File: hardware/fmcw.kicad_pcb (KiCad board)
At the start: 4 copper layers, 123.2 x 49.5 mm, 450 parts, among them CON2 BARREL_JACK, J1 SD_Card, J2 USB_B_Micro, P1 SMA, P10 CONN_01X01, P11 CONN_01X01, P12 CONN_01X01, P13 CONN_01X01, P14 CONN_01X01, P15 CONN_01X01, P16 CONN_01X01, P2 SMA, P3 CONN_02X04, P4 CONN_02X04, P5 CONN_01X01, P6 CONN_01X01, P7 CONN_01X01, P8 CONN_01X01, P9 CONN_01X01, Q1 RE1C002UN, Q2 DNP(RE1C002UN), SW2 SW_PUSH, U1 ADF4158, U10 HMC431LP4, U11 SKY65404, U12 PAT1220-6dB, U13 TRF37A73, U14 FT2232H, U15 SMA, U16 SKY65404, U17 SE5004L, U18 TPS5420D, U19 TPS5420D, U2 LP5907-1.8, U20 LP5907-3.0, U21 LP2985A-10DBVR, U22 TPS7A91, U23 TPS7A91, U24 TPS7A91, U25 MIC5301-3.3, U26 5400BL15B050E, U27 5400BL15B050E, U28 5400BL15B050E, U29 ADL5802, U3 PAT1220-6dB, U31 93LCxxB, U32 TPS7A7200RGW, U34 ADA4940-2, U35 ADA4940-2, U37 SE2567L, U38 TPS7A91, U39 LP5907-3.0, U4 KT2520K, U40 W25Q32JV, U5 NC7S04P5X, U6 NB3N551, U7 TLV172DCK, U8 LTC2292, U9 TRF37A73, Y1 ABM10-167-12.000MHZ-T3

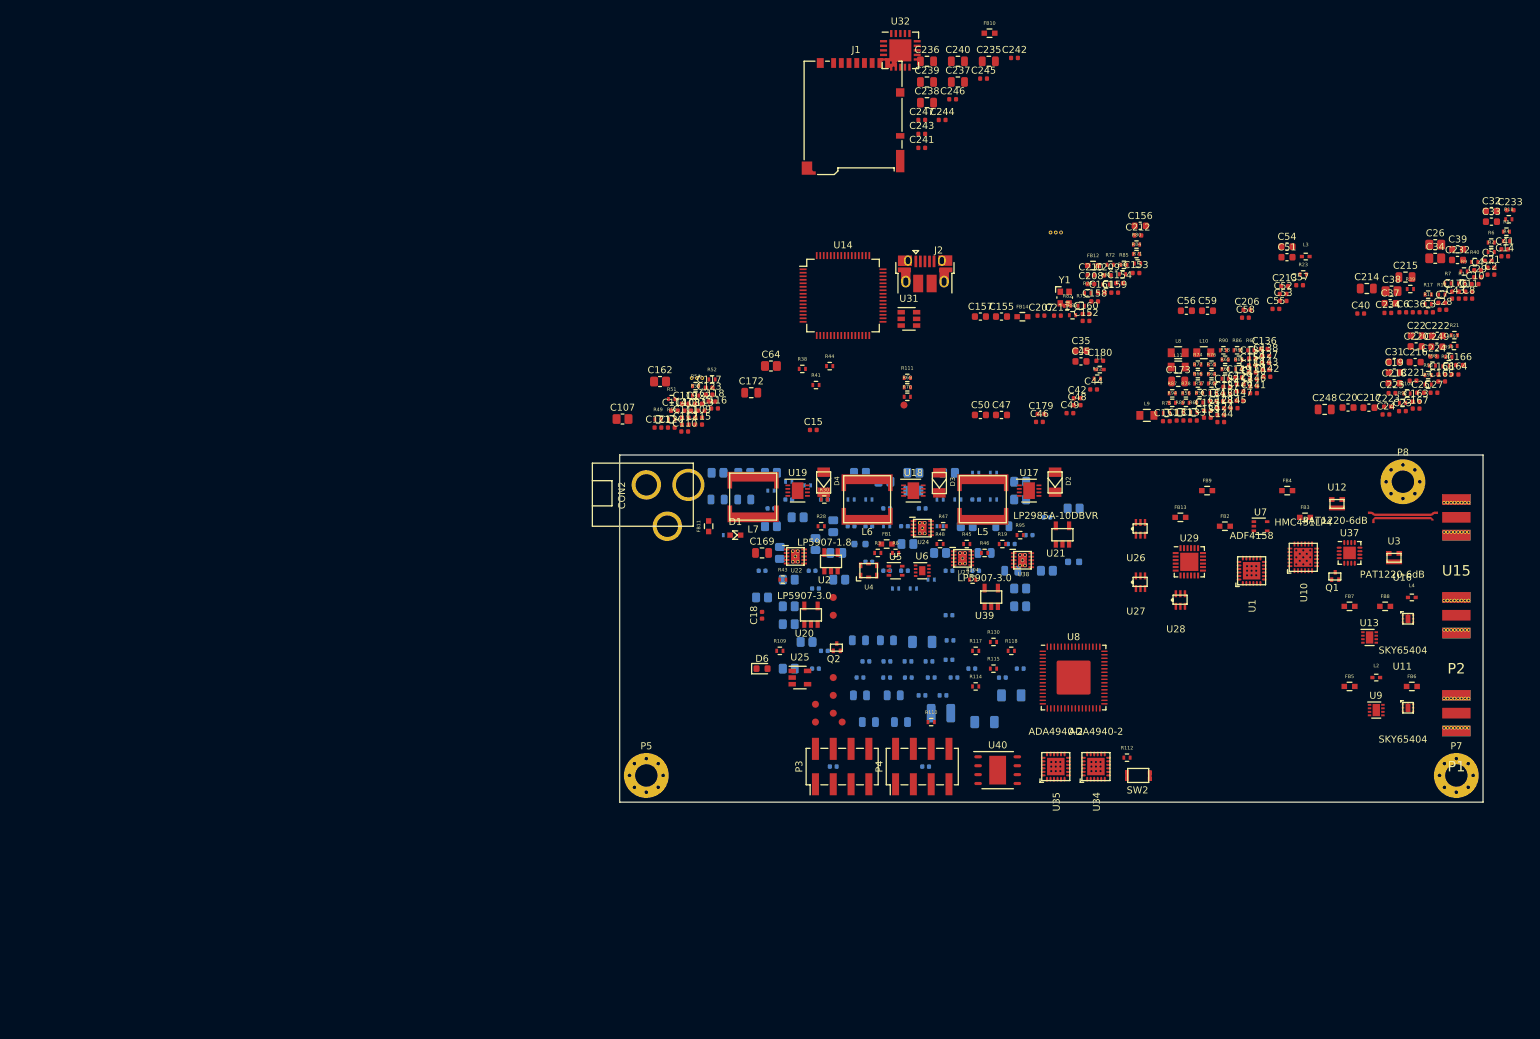
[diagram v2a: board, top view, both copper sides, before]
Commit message: Added MFNs to components.
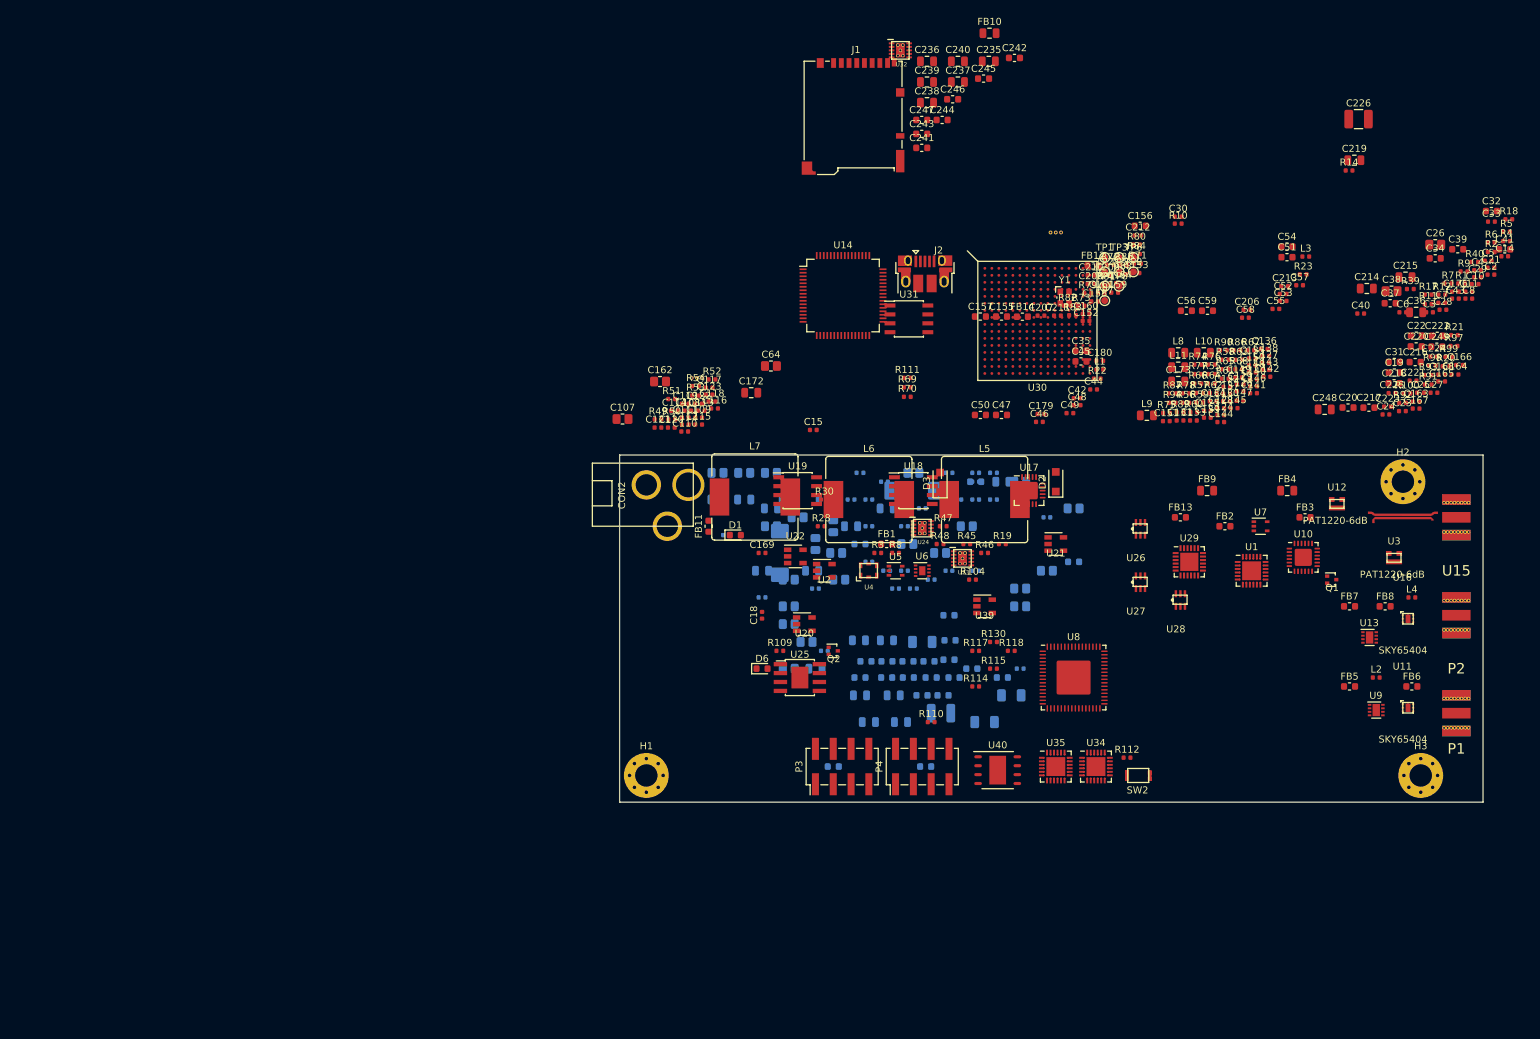
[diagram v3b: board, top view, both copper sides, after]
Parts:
- removed C227, C230: 10u, Capacitor_SMD:C_0805_2012Metric
- removed C228: 100n, Capacitor_SMD:C_0402_1005Metric
- removed C229: 10n, Capacitor_SMD:C_0402_1005Metric
- removed C231: DNP, Capacitor_SMD:C_0805_2012Metric
- removed C232: 2.2u, Capacitor_SMD:C_0603_1608Metric
- removed C233, C234: 100p, Capacitor_SMD:C_0402_1005Metric
- removed D4: SS13FL, fmcw:SOD-123F
- removed P10, P11, P12, P13, P14, P15, P16, P6, P9: CONN_01X01, fmcw:TP_1.00
- removed P5, P7, P8: CONN_01X01, fmcw:MountingHole_3.2mm_M3_Pad_Via_mod
- removed R101: DNP, fmcw:R_0402b
- removed R103: 0, fmcw:R_0402b
- removed R34, R36: 4.99k, fmcw:R_0402b
- removed R35: 1k, fmcw:R_0402b
- removed R37: 590, fmcw:R_0402b
- removed R38: 33, fmcw:R_0402b
- removed R41: 56, fmcw:R_0402b
- removed R42: 100, fmcw:R_0402b
- removed R43: 10.5k, fmcw:R_0402b
- removed R44: 2k, fmcw:R_0402b
- removed R95: 1.47k, fmcw:R_0402b
- removed U37: SE2567L, Package_DFN_QFN:QFN-16-1EP_3x3mm_P0.5mm_EP1.8x1.8mm
- removed U38: TPS7A91, fmcw:SON-10_2.5x2.5mm
- added C219: DNP, Capacitor_SMD:C_0805_2012Metric, F.Cu at (215.3, 32.9)
- added C226: 47u, Capacitor_SMD:C_1210_3225Metric, F.Cu at (215.9, 27.0)
- added C30: 10p, Capacitor_SMD:C_0402_1005Metric, F.Cu at (190.2, 40.9)
- added H1: MountingHole_Pad, MountingHole:MountingHole_3.2mm_M3_Pad_Via, F.Cu at (114.3, 120.7)
- added H2: MountingHole_Pad, MountingHole:MountingHole_3.2mm_M3_Pad_Via, F.Cu at (222.2, 78.7)
- added H3: MountingHole_Pad, MountingHole:MountingHole_3.2mm_M3_Pad_Via, F.Cu at (224.8, 120.7)
- added R10: 10k, Resistor_SMD:R_0402_1005Metric, F.Cu at (190.2, 41.9)
- added R14: 10k, Resistor_SMD:R_0402_1005Metric, F.Cu at (214.6, 34.3)
- added TP1: TestPoint, TestPoint:TestPoint_Pad_D1.0mm, F.Cu at (179.7, 46.7)
- added TP2: TestPoint, TestPoint:TestPoint_Pad_D1.0mm, F.Cu at (179.7, 48.8)
- added TP3: TestPoint, TestPoint:TestPoint_Pad_D1.0mm, F.Cu at (181.7, 46.7)
- added TP4: TestPoint, TestPoint:TestPoint_Pad_D1.0mm, F.Cu at (179.7, 50.8)
- added TP5: TestPoint, TestPoint:TestPoint_Pad_D1.0mm, F.Cu at (181.7, 48.8)
- added TP6: TestPoint, TestPoint:TestPoint_Pad_D1.0mm, F.Cu at (183.8, 46.7)
- added TP7: TestPoint, TestPoint:TestPoint_Pad_D1.0mm, F.Cu at (179.7, 52.9)
- added TP8: TestPoint, TestPoint:TestPoint_Pad_D1.0mm, F.Cu at (181.7, 50.8)
- added TP9: TestPoint, TestPoint:TestPoint_Pad_D1.0mm, F.Cu at (183.8, 48.8)
- added U30: XC7A15T-FTG256, fmcw:FTG256, F.Cu at (170.1, 55.8)
- C100: value 10u -> 100n; footprint Capacitor_SMD:C_0805_2012Metric -> Capacitor_SMD:C_0402_1005Metric
- C103, C86: value DNP -> 10u
- C106: value 10u -> DNP
- C169: value DNP -> 10n; footprint Capacitor_SMD:C_0805_2012Metric -> Capacitor_SMD:C_0402_1005Metric
- C170, C171, C187, C189, C190, C191, C192, C193, C197, C198, C199, C200, C201, C202, C203, C204, C205, C241, C242, C243, C244, C245, C246, C247, C251, C41, C63, C66: footprint Capacitor_SMD:C_0402_1005Metric -> Capacitor_SMD:C_0603_1608Metric
- C175, C96: value DNP -> 10u; footprint Capacitor_SMD:C_0402_1005Metric -> Capacitor_SMD:C_0805_2012Metric
- C33: footprint Capacitor_SMD:C_0603_1608Metric -> Capacitor_SMD:C_0402_1005Metric
- C34: footprint Capacitor_SMD:C_0805_2012Metric -> Capacitor_SMD:C_0603_1608Metric
- C36, C65, C69, C73, C74, C75, C90: footprint Capacitor_SMD:C_0402_1005Metric -> Capacitor_SMD:C_0805_2012Metric
- C60, C61, C77, C78: footprint Capacitor_SMD:C_0805_2012Metric -> Capacitor_SMD:C_0402_1005Metric
- C79, C80: value 6TPH100MAEA -> 100u; footprint Capacitor_SMD:C_0805_2012Metric -> Capacitor_Tantalum_SMD:CP_EIA-7343-31_Kemet-D
- C82: value 10n -> 100n
- C83: value 100n -> 10u
- C84: value 10n -> 10u
- D1: value LED -> Red; footprint fmcw:LED_0603 -> LED_SMD:LED_0603_1608Metric
- D2, D3: footprint fmcw:SOD-123F -> Diode_SMD:D_SOD-123F
- D6: value LED -> Red
- FB1, FB12, FB13, FB14, FB2, FB3, FB5, FB6, FB7, FB8: value BLM18PG181SN1D -> BLM18PG181SH1D; footprint fmcw:C_0603b -> Inductor_SMD:L_0603_1608Metric
- FB10, FB4, FB9: footprint fmcw:C_0603b -> Inductor_SMD:L_0805_2012Metric
- FB11: value CIC21P101NE -> 74279228600; footprint fmcw:C_0603b -> Inductor_SMD:L_0603_1608Metric
- L1, L2, L3, L4: footprint fmcw:C_0402b -> Inductor_SMD:L_0402_1005Metric
- L10, L11, L8, L9: footprint fmcw:C_0805b -> Inductor_SMD:L_0805_2012Metric
- L5, L7: value SRR1210A-330M -> 33u; footprint fmcw:SRR6040A -> Inductor_SMD:L_Bourns_SRR1210A
- L6: value 33u (SRR6040A-330M) -> 33u; footprint fmcw:SRR6040A -> Inductor_SMD:L_Bourns_SRR1210A
- Q1, Q2: footprint fmcw:SOT-416 -> Package_TO_SOT_SMD:SOT-416
- R1, R100, R104, R109, R11, R110, R111, R112, R114, R115, R117, R118, R12, R13, R130, R15, R16, R17, R18, R19, R2, R20, R21, R22, R23, R24, R25, R26, R3, R39, R40, R45, R46, R47, R48, R49, R5, R50, R51, R52, R53, R54, R59, R6, R60, R61, R62, R63, R64, R65, R66, R67, R68, R69, R7, R70, R71, R72, R73, R74, R75, R76, R77, R78, R79, R8, R80, R81, R82, R83, R84, R85, R86, R87, R88, R89, R9, R90, R91, R92, R93, R94, R97, R98, R99: footprint fmcw:R_0402b -> Resistor_SMD:R_0402_1005Metric
- R27: value 100k -> 33; footprint fmcw:R_0402b -> Resistor_SMD:R_0402_1005Metric
- R28: value 2.55k -> 4.99k; footprint fmcw:R_0402b -> Resistor_SMD:R_0402_1005Metric
- R29: value 10.2k -> 20k; footprint fmcw:R_0402b -> Resistor_SMD:R_0402_1005Metric
- R30: value 280k -> 274k; footprint fmcw:R_0402b -> Resistor_SMD:R_0402_1005Metric
- R31: value 30.9k -> 30.1k; footprint fmcw:R_0402b -> Resistor_SMD:R_0402_1005Metric
- R32: value 4.99k -> 3.57k; footprint fmcw:R_0402b -> Resistor_SMD:R_0402_1005Metric
- R33: value 7.5k -> 1.15k; footprint fmcw:R_0402b -> Resistor_SMD:R_0402_1005Metric
- R4: value 3.1k -> 3.09k; footprint fmcw:R_0402b -> Resistor_SMD:R_0402_1005Metric
- R55, R56, R57, R58: value 550 -> 549; footprint fmcw:R_0402b -> Resistor_SMD:R_0402_1005Metric
- U1, U34, U35: footprint fmcw:VFQFN-24 -> Package_DFN_QFN:WQFN-24-1EP_4x4mm_P0.5mm_EP2.7x2.7mm
- U10: footprint fmcw:VQFN-24 -> Package_DFN_QFN:VQFN-24-1EP_4x4mm_P0.5mm_EP2.45x2.45mm
- U17: footprint Package_DFN_QFN:DFN-8-1EP_3x3mm_P0.5mm_EP1.66x2.38mm -> Package_DFN_QFN:QFN-20-1EP_4x4mm_P0.5mm_EP2.5x2.5mm
- U18, U19: footprint Package_DFN_QFN:DFN-8-1EP_3x3mm_P0.5mm_EP1.66x2.38mm -> Package_SO:SOIC-8_3.9x4.9mm_P1.27mm
- U2, U20, U21, U39: footprint fmcw:SOT-23-5 -> Package_TO_SOT_SMD:SOT-23-5
- U22: value TPS7A91 -> TPS560200; footprint fmcw:SON-10_2.5x2.5mm -> Package_TO_SOT_SMD:SOT-23-5
- U25: value MIC5301-3.3 -> TPS7A7001DDA; footprint Package_TO_SOT_SMD:SOT-23-5 -> Package_SO:TI_SO-PowerPAD-8
- U31: footprint Package_TO_SOT_SMD:SOT-23-6 -> Package_SO:SOIC-8_3.9x4.9mm_P1.27mm
- U32: value TPS7A7200RGW -> TPS7A91; footprint Package_DFN_QFN:Texas_VQFN-RGW-20 -> fmcw:SON-10_2.5x2.5mm
- Y1: value ABM10-167-12.000MHZ-T3 -> 12MHz
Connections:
- C100 pad 1: /5V -> Net-(C100-Pad1)
- C106 pad 1: /3V3D -> /5V
- C169 pad 1: /power/5V6 -> /3V3D
- C169 pad 2: GND -> Net-(C169-Pad2)
- C175 pad 1: Net-(C175-Pad1) -> /3V3D
- C81 pad 1: /power/3V6 -> /power/12V
- C82 pad 1: /power/5V6 -> /power/12V
- C83 pad 1: Net-(C83-Pad1) -> /1V0
- C84 pad 2: Net-(C84-Pad2) -> GND
- C86 pad 1: /5V -> /1V0
- C86 pad 2: Net-(C86-Pad2) -> GND
- C94 pad 1: /power/3V6 -> /power/5V6
- C96 pad 1: /1V0 -> /power/3V6
- J1 pad 1: /fpga/SD_DAT3 -> /fpga/SD_DAT2
- J1 pad 2: /fpga/SD_CMD -> /fpga/SD_DAT3
- J1 pad 3: GND -> /fpga/SD_CMD
- J1 pad 9: /fpga/SD_DAT2 -> GND
- J2 pad 4: Net-(J2-Pad4) -> (no net)
- L6 pad 1: Net-(D3-Pad1) -> Net-(L6-Pad1)
- L6 pad 2: /3V6 -> /1V0
- R27 pad 2: /5V -> Net-(C13-Pad1)
- R28 pad 2: Net-(C84-Pad2) -> Net-(R28-Pad2)
- R29 pad 1: Net-(C84-Pad2) -> Net-(R28-Pad2)
- R3 pad 2: Net-(C13-Pad1) -> Net-(R27-Pad1)
- R30 pad 2: Net-(C86-Pad2) -> Net-(R30-Pad2)
- R31 pad 1: Net-(C86-Pad2) -> Net-(R30-Pad2)
- R32 pad 1: /1V0 -> /3V3D
- R32 pad 2: Net-(C63-Pad2) -> Net-(C169-Pad2)
- R33 pad 1: Net-(C63-Pad2) -> Net-(C169-Pad2)
- U1 pad 21: Net-(U1-Pad21) -> (no net)
- U14 pad 34: Net-(U14-Pad34) -> (no net)
- U14 pad 43: Net-(U14-Pad43) -> (no net)
- U14 pad 44: Net-(U14-Pad44) -> (no net)
- U14 pad 45: Net-(U14-Pad45) -> (no net)
- U14 pad 46: Net-(U14-Pad46) -> (no net)
- U14 pad 48: Net-(U14-Pad48) -> (no net)
- U14 pad 52: Net-(U14-Pad52) -> (no net)
- U14 pad 53: Net-(U14-Pad53) -> (no net)
- U14 pad 54: Net-(U14-Pad54) -> (no net)
- U14 pad 55: Net-(U14-Pad55) -> (no net)
- U14 pad 57: Net-(U14-Pad57) -> (no net)
- U14 pad 58: Net-(U14-Pad58) -> (no net)
- U14 pad 60: Net-(U14-Pad60) -> (no net)
- U17 pad 1: Net-(U17-Pad1) -> (no net)
- U18 pad 2: Net-(U18-Pad2) -> (no net)
- U18 pad 3: Net-(U18-Pad3) -> (no net)
- U18 pad 5: Net-(U18-Pad5) -> (no net)
- U19 pad 2: Net-(U19-Pad2) -> (no net)
- U19 pad 3: Net-(U19-Pad3) -> (no net)
- U19 pad 5: Net-(U19-Pad5) -> (no net)
- U22 pad 1: /1V0 -> (no net)
- U22 pad 2: /1V0 -> GND
- U22 pad 3: Net-(C84-Pad2) -> Net-(L6-Pad1)
- U22 pad 4: GND -> /power/12V
- U22 pad 5: Net-(U22-Pad5) -> Net-(R28-Pad2)
- U24 pad 5: Net-(U24-Pad5) -> (no net)
- U25 pad 1: /power/3V6 -> (no net)
- U25 pad 2: GND -> /power/5V6
- U25 pad 3: Net-(R104-Pad2) -> /power/5V6
- U25 pad 4: Net-(C175-Pad1) -> (no net)
- U25 pad 5: /3V3D -> (no net)
- U31 pad 6: Net-(U31-Pad6) -> (no net)
- U32 pad 1: /5V -> /3V3D
- U32 pad 10: Net-(U32-Pad10) -> /power/3V6
- U32 pad 11: Net-(U32-Pad11) -> GND
- U32 pad 2: Net-(U32-Pad2) -> /3V3D
- U32 pad 3: Net-(C86-Pad2) -> Net-(C169-Pad2)
- U32 pad 4: Net-(R27-Pad1) -> GND
- U32 pad 5: Net-(U32-Pad5) -> (no net)
- U32 pad 6: Net-(U32-Pad6) -> /power/3V6
- U32 pad 7: Net-(U32-Pad7) -> Net-(R104-Pad2)
- U32 pad 8: GND -> Net-(C100-Pad1)
- U32 pad 9: Net-(U32-Pad9) -> /power/3V6
- U5 pad 2: Net-(C13-Pad1) -> Net-(R27-Pad1)
- U6 pad 5: Net-(U6-Pad5) -> (no net)
- U8 pad 24: Net-(U8-Pad24) -> (no net)
- U8 pad 25: Net-(U8-Pad25) -> (no net)
- U8 pad 26: Net-(U8-Pad26) -> (no net)
- U8 pad 27: Net-(U8-Pad27) -> (no net)
- U8 pad 28: Net-(U8-Pad28) -> (no net)
- U8 pad 29: Net-(U8-Pad29) -> (no net)
- U8 pad 30: Net-(U8-Pad30) -> (no net)
- U8 pad 33: Net-(U8-Pad33) -> (no net)
- U8 pad 34: Net-(U8-Pad34) -> (no net)
- U8 pad 35: Net-(U8-Pad35) -> (no net)
- U8 pad 36: Net-(U8-Pad36) -> (no net)
- U8 pad 37: Net-(U8-Pad37) -> (no net)
- U8 pad 38: Net-(U8-Pad38) -> (no net)
- U8 pad 39: Net-(U8-Pad39) -> (no net)
- U8 pad 41: Net-(U8-Pad41) -> (no net)
- U8 pad 42: Net-(U8-Pad42) -> (no net)

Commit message: Fixed ERC errors.
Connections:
- C79 pad 1: /power/3V6 -> /3V6
- C85 pad 1: /power/3V6 -> /3V6
- C87 pad 1: /power/3V6 -> /3V6
- C88 pad 1: /power/3V6 -> /3V6
- C96 pad 1: /power/3V6 -> /3V6
- L5 pad 2: /power/3V6 -> /3V6
- R104 pad 1: /power/3V6 -> /3V6
- R14 pad 1: /power/3V6 -> /3V6
- R24 pad 1: /power/3V6 -> /3V6
- U20 pad 1: /power/3V6 -> /3V6
- U20 pad 3: /power/3V6 -> /3V6
- U23 pad 10: /power/3V6 -> /3V6
- U23 pad 6: /power/3V6 -> /3V6
- U23 pad 9: /power/3V6 -> /3V6
- U24 pad 10: /power/3V6 -> /3V6
- U24 pad 6: /power/3V6 -> /3V6
- U24 pad 7: /power/3V6 -> /3V6
- U24 pad 9: /power/3V6 -> /3V6
- U32 pad 10: /power/3V6 -> /3V6
- U32 pad 6: /power/3V6 -> /3V6
- U32 pad 9: /power/3V6 -> /3V6

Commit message: Finished design, began routing.
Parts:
- removed CON2: BARREL_JACK, fmcw:EJ508A
- removed D6: Red, LED_SMD:LED_0603_1608Metric
- removed F1, F2: Via, fmcw:RF_via
- removed P3, P4: CONN_02X04, Connector_PinHeader_2.54mm:PinHeader_2x04_P2.54mm_Vertical_SMD
- removed R100, R97, R98, R99: 49.9, Resistor_SMD:R_0402_1005Metric
- removed R104: 68k, Resistor_SMD:R_0402_1005Metric
- removed R109: 240, Resistor_SMD:R_0402_1005Metric
- removed R110, R86, R92: DNP, Resistor_SMD:R_0402_1005Metric
- removed R111: 1k, Resistor_SMD:R_0402_1005Metric
- removed R112, R117, R118, R82: 4.7k, Resistor_SMD:R_0402_1005Metric
- removed R114, R115, R81, R87, R89, R90, R91, R93, R94: 0, Resistor_SMD:R_0402_1005Metric
- removed R130, R84, R85, R88: 33, Resistor_SMD:R_0402_1005Metric
- removed R83: 10k, Resistor_SMD:R_0402_1005Metric
- removed SW2: SW_PUSH, fmcw:EVP-AWBA2A
- removed U21: LP2985A-10DBVR, Package_TO_SOT_SMD:SOT-23-5
- removed U40: W25Q32JV, Package_DFN_QFN:DFN-S-8-1EP_6x5mm_P1.27mm
- removed Z1: 15dB COUPLER, fmcw:coupler
- added C227: 100p, Capacitor_SMD:C_0402_1005Metric, F.Cu at (90.3, 44.8)
- added C228: 10u, Capacitor_SMD:C_0805_2012Metric, F.Cu at (82.7, 48.0)
- added C229: 100n, Capacitor_SMD:C_0402_1005Metric, F.Cu at (94.1, 44.2)
- added C230: 100n, Capacitor_SMD:C_0402_1005Metric, F.Cu at (88.7, 48.3)
- added C231: 100n, Capacitor_SMD:C_0402_1005Metric, F.Cu at (90.6, 48.3)
- added C232: 100n, Capacitor_SMD:C_0402_1005Metric, F.Cu at (92.5, 46.8)
- added C233: 100n, Capacitor_SMD:C_0402_1005Metric, F.Cu at (110.9, 77.9)
- added C234: 100n, Capacitor_SMD:C_0402_1005Metric, F.Cu at (114.3, 79.9)
- added C250: 100n, Capacitor_SMD:C_0402_1005Metric, F.Cu at (36.2, 30.7)
- added CON1: BARREL_JACK, Connector_BarrelJack:BarrelJack_Wuerth_6941xx301002, F.Cu at (94.5, 93.5)
- added D4: SS24FL, fmcw:SOD-123F, F.Cu at (158.0, 91.7)
- added FB15: 74279228600, Inductor_SMD:L_0603_1608Metric, F.Cu at (99.8, 93.2)
- added FB16: BLM18PG181SH1D, Inductor_SMD:L_0603_1608Metric, F.Cu at (87.8, 45.1)
- added J3: SMA, fmcw:CONSMA003.062, F.Cu at (231.9, 102.9)
- added J4: SMA, fmcw:CONSMA003.062, F.Cu at (231.9, 133.6)
- added J5: SMA, fmcw:CONSMA003.062, F.Cu at (231.9, 117.9)
- added R34: 0, Resistor_SMD:R_0402_1005Metric, F.Cu at (92.0, 84.7)
- added R35: 0, Resistor_SMD:R_0402_1005Metric, F.Cu at (98.8, 78.6)
- added R36: 22, Resistor_SMD:R_0402_1005Metric, F.Cu at (93.9, 80.7)
- added R37: 5.49k, Resistor_SMD:R_0402_1005Metric, F.Cu at (109.6, 27.9)
- added R38: DNP, Resistor_SMD:R_0402_1005Metric, F.Cu at (102.2, 34.8)
- added R41: 4.7k, Resistor_SMD:R_0402_1005Metric, F.Cu at (100.3, 35.7)
- added R42: 4.7k, Resistor_SMD:R_0402_1005Metric, F.Cu at (106.5, 30.1)
- added R43: 47k, Resistor_SMD:R_0402_1005Metric, F.Cu at (107.7, 28.9)
- added R44: DNP, Resistor_SMD:R_0402_1005Metric, F.Cu at (110.5, 25.5)
- added SW1: SW_PUSH, fmcw:EVP-AWBA2A, F.Cu at (36.3, 45.3)
- added U33: LP5907MFX-3.0, Package_TO_SOT_SMD:SOT-23-5, F.Cu at (64.1, 62.2)
- added U36: 5400BL15B050E, RF_Converter:Balun_Johanson_5400BL15B050E, F.Cu at (86.1, 48.3)
- added U37: 5400BL15B050E, RF_Converter:Balun_Johanson_5400BL15B050E, F.Cu at (91.3, 43.0)
- added U38: ADL5802, Package_CSP:LFCSP-24-1EP_4x4mm_P0.5mm_EP2.5x2.5mm, F.Cu at (83.6, 44.4)
- C1, C100, C175, C75, C89, C9, C91: moved to F.Cu
- C10: value 2.2n -> 4.7u; footprint Capacitor_SMD:C_0402_1005Metric -> Capacitor_SMD:C_0603_1608Metric
- C101, C102, C62, C65, C69, C70, C73, C74, C85, C86, C96, C98: value 10u -> 100n; footprint Capacitor_SMD:C_0805_2012Metric -> Capacitor_SMD:C_0402_1005Metric; moved to F.Cu
- C103: value 10u -> 10p; footprint Capacitor_SMD:C_0805_2012Metric -> Capacitor_SMD:C_0402_1005Metric; moved to F.Cu
- C104, C105, C71, C72: value DNP -> 100n; footprint Capacitor_SMD:C_0805_2012Metric -> Capacitor_SMD:C_0402_1005Metric; moved to F.Cu
- C106: value DNP -> 10p; footprint Capacitor_SMD:C_0805_2012Metric -> Capacitor_SMD:C_0402_1005Metric; moved to F.Cu
- C107: value DNP -> 10p; footprint Capacitor_SMD:C_0805_2012Metric -> Capacitor_SMD:C_0402_1005Metric
- C109, C112: value 3p -> 10p
- C11, C3, C8: value 10p -> 100n
- C110: value 3p -> 2.2n
- C111, C113: value 3p -> 100n
- C114: value 3p -> 51p
- C117, C165, C167, C168: value 100p -> 100n
- C118, C213: value 100p -> 10u; footprint Capacitor_SMD:C_0402_1005Metric -> Capacitor_SMD:C_0805_2012Metric
- C119, C180: value 100p -> 10n
- C12: value 1u -> 100n; footprint Capacitor_SMD:C_0603_1608Metric -> Capacitor_SMD:C_0402_1005Metric; moved to F.Cu
- C120: value 100n -> 68p
- C124, C148: value DNP -> 10p
- C125, C143, C144, C145, C146: value DNP -> 100n
- C126: value 2.2n -> 100n
- C127: value 2.2n -> 10p
- C128: value 10n -> DNP; footprint Capacitor_SMD:C_0402_1005Metric -> Capacitor_SMD:C_0603_1608Metric
- C129, C169, C206: value 10n -> 10u; footprint Capacitor_SMD:C_0402_1005Metric -> Capacitor_SMD:C_0805_2012Metric
- C13, C95, C97, C99: value 10n -> 100n; moved to F.Cu
- C130: value 10n -> 2.2u; footprint Capacitor_SMD:C_0402_1005Metric -> Capacitor_SMD:C_0603_1608Metric
- C131: value 10n -> 100p
- C132, C138, C151: value 100n -> DNP; footprint Capacitor_SMD:C_0402_1005Metric -> Capacitor_SMD:C_0603_1608Metric
- C133, C139, C2, C207, C210: value 100n -> 10u; footprint Capacitor_SMD:C_0402_1005Metric -> Capacitor_SMD:C_0805_2012Metric
- C134: value 10p -> 2.2u; footprint Capacitor_SMD:C_0402_1005Metric -> Capacitor_SMD:C_0603_1608Metric
- C135, C136: value 10p -> 100p
- C137: value 10p -> DNP; footprint Capacitor_SMD:C_0402_1005Metric -> Capacitor_SMD:C_0603_1608Metric
- C14: value 51p -> 470n; footprint Capacitor_SMD:C_0402_1005Metric -> Capacitor_SMD:C_0603_1608Metric
- C140: value DNP -> 2.2u; footprint Capacitor_SMD:C_0402_1005Metric -> Capacitor_SMD:C_0603_1608Metric
- C141, C142: value DNP -> 100p
- C147: value DNP -> 18p
- C149: value DNP -> 10n
- C15, C43, C49: value 100n -> 470n; footprint Capacitor_SMD:C_0402_1005Metric -> Capacitor_SMD:C_0603_1608Metric
- C150, C225: value 100n -> 100p
- C152, C159: value 100n -> 18p
- C154: value 100n -> 0.5p
- C155, C156, C157: value 4.7u -> 100n; footprint Capacitor_SMD:C_0603_1608Metric -> Capacitor_SMD:C_0402_1005Metric
- C16: value 10n -> 470n; footprint Capacitor_SMD:C_0402_1005Metric -> Capacitor_SMD:C_0603_1608Metric; moved to F.Cu
- C160: value 100n -> 10p
- C161, C211, C4: value 100n -> 10n
- C162: value 10u -> 100p; footprint Capacitor_SMD:C_0805_2012Metric -> Capacitor_SMD:C_0402_1005Metric
- C163: value 100p -> DNP; footprint Capacitor_SMD:C_0402_1005Metric -> Capacitor_SMD:C_0603_1608Metric
- C164: value 100p -> 18p
- C166: value 100p -> 0.5p
- C17: value 100n -> DNP; moved to F.Cu
- C170, C171, C187, C192, C193, C199, C200, C201: value 470n -> 10u; footprint Capacitor_SMD:C_0603_1608Metric -> Capacitor_SMD:C_0805_2012Metric; moved to F.Cu
- C172, C173: value DNP -> 10u
- C174: value DNP -> 10u; footprint Capacitor_SMD:C_0402_1005Metric -> Capacitor_SMD:C_0805_2012Metric; moved to F.Cu
- C177: value DNP -> 1u; footprint Capacitor_SMD:C_0805_2012Metric -> Capacitor_SMD:C_0603_1608Metric; moved to F.Cu
- C178: value DNP -> 10u; moved to F.Cu
- C181: value 100u -> 10u; footprint Capacitor_SMD:C_1210_3225Metric -> Capacitor_SMD:C_0805_2012Metric; moved to F.Cu
- C182, C196: value 47u -> 10u; footprint Capacitor_SMD:C_1206_3216Metric -> Capacitor_SMD:C_0805_2012Metric; moved to F.Cu
- C183, C194, C195: value 4.7u -> 10u; moved to F.Cu
- C184: value 47u -> 10n; footprint Capacitor_SMD:C_1206_3216Metric -> Capacitor_SMD:C_0402_1005Metric; moved to F.Cu
- C185, C186, C188: value 4.7u -> DNP; moved to F.Cu
- C189, C202: value 470n -> DNP; footprint Capacitor_SMD:C_0603_1608Metric -> Capacitor_SMD:C_0805_2012Metric; moved to F.Cu
- C19, C217: value 1u -> 100n; footprint Capacitor_SMD:C_0603_1608Metric -> Capacitor_SMD:C_0402_1005Metric
- C190, C191: value 470n -> 100u; footprint Capacitor_SMD:C_0603_1608Metric -> Capacitor_Tantalum_SMD:CP_EIA-7343-31_Kemet-D; moved to F.Cu
- C197, C198, C203: value 470n -> 100n; footprint Capacitor_SMD:C_0603_1608Metric -> Capacitor_SMD:C_0402_1005Metric; moved to F.Cu
- C20: value 1u -> 47u; footprint Capacitor_SMD:C_0603_1608Metric -> Capacitor_SMD:C_1206_3216Metric
- C204, C205: value 470n -> 10n; footprint Capacitor_SMD:C_0603_1608Metric -> Capacitor_SMD:C_0402_1005Metric; moved to F.Cu
- C208, C209: value 15p -> DNP; footprint Capacitor_SMD:C_0402_1005Metric -> Capacitor_SMD:C_0805_2012Metric
- C21, C23, C24, C25, C27: value 100n -> 4.7u; footprint Capacitor_SMD:C_0402_1005Metric -> Capacitor_SMD:C_0805_2012Metric
- C212: value 100n -> DNP; footprint Capacitor_SMD:C_0402_1005Metric -> Capacitor_SMD:C_0805_2012Metric
- C215: value DNP -> 100n; footprint Capacitor_SMD:C_0805_2012Metric -> Capacitor_SMD:C_0402_1005Metric
- C216: value 2.2u -> 100n; footprint Capacitor_SMD:C_0603_1608Metric -> Capacitor_SMD:C_0402_1005Metric
- C218, C222: value 1u -> 3p; footprint Capacitor_SMD:C_0603_1608Metric -> Capacitor_SMD:C_0402_1005Metric
- C219: value DNP -> 3p; footprint Capacitor_SMD:C_0805_2012Metric -> Capacitor_SMD:C_0402_1005Metric
- C22: value 2.2u -> 47u; footprint Capacitor_SMD:C_0603_1608Metric -> Capacitor_SMD:C_1206_3216Metric
- C220: value 2.2u -> 3p; footprint Capacitor_SMD:C_0603_1608Metric -> Capacitor_SMD:C_0402_1005Metric
- C221, C223: value 100n -> 3p
- C226: value 47u -> 100p; footprint Capacitor_SMD:C_1210_3225Metric -> Capacitor_SMD:C_0402_1005Metric
- C235: value 4.7u -> DNP
- C236, C237: value 4.7u -> DNP; footprint Capacitor_SMD:C_0805_2012Metric -> Capacitor_SMD:C_0402_1005Metric
- C238, C239: value 4.7u -> 2.2n; footprint Capacitor_SMD:C_0805_2012Metric -> Capacitor_SMD:C_0402_1005Metric
- C240: value 4.7u -> 10n; footprint Capacitor_SMD:C_0805_2012Metric -> Capacitor_SMD:C_0402_1005Metric
- C241, C242, C243: value 470n -> 10n; footprint Capacitor_SMD:C_0603_1608Metric -> Capacitor_SMD:C_0402_1005Metric
- C244, C245: value 470n -> 100n; footprint Capacitor_SMD:C_0603_1608Metric -> Capacitor_SMD:C_0402_1005Metric
- C246, C247: value 470n -> 10p; footprint Capacitor_SMD:C_0603_1608Metric -> Capacitor_SMD:C_0402_1005Metric
- C248: value 10u -> 10p; footprint Capacitor_SMD:C_0805_2012Metric -> Capacitor_SMD:C_0402_1005Metric
- C249: value 1u -> 10p; footprint Capacitor_SMD:C_0603_1608Metric -> Capacitor_SMD:C_0402_1005Metric
- C251: value 470n -> 10p; footprint Capacitor_SMD:C_0603_1608Metric -> Capacitor_SMD:C_0402_1005Metric; moved to F.Cu
- C252: value 100n -> 10p; moved to F.Cu
- C26: value 10u -> 4.7u
- C28: value 10n -> 4.7u; footprint Capacitor_SMD:C_0402_1005Metric -> Capacitor_SMD:C_0805_2012Metric
- C29: value 68p -> 4.7u; footprint Capacitor_SMD:C_0402_1005Metric -> Capacitor_SMD:C_0805_2012Metric
- C30, C33, C53: value 10p -> 470n; footprint Capacitor_SMD:C_0402_1005Metric -> Capacitor_SMD:C_0603_1608Metric
- C31, C41: value 2.2u -> 4.7u; footprint Capacitor_SMD:C_0603_1608Metric -> Capacitor_SMD:C_0805_2012Metric
- C32: value DNP -> 4.7u; footprint Capacitor_SMD:C_0603_1608Metric -> Capacitor_SMD:C_0805_2012Metric
- C34, C35, C37, C45, C47, C50, C51, C54, C56: value DNP -> 470n
- C36: value 10u -> 470n; footprint Capacitor_SMD:C_0805_2012Metric -> Capacitor_SMD:C_0603_1608Metric
- C38: value 10u -> 100u; footprint Capacitor_SMD:C_0805_2012Metric -> Capacitor_SMD:C_1210_3225Metric
- C39: value 2.2u -> 470n
- C40: value 100p -> 470n; footprint Capacitor_SMD:C_0402_1005Metric -> Capacitor_SMD:C_0603_1608Metric
- C42, C46, C55: value 18p -> 470n; footprint Capacitor_SMD:C_0402_1005Metric -> Capacitor_SMD:C_0603_1608Metric
- C44: value 10p -> 4.7u; footprint Capacitor_SMD:C_0402_1005Metric -> Capacitor_SMD:C_0805_2012Metric
- C48, C57: value 0.5p -> 470n; footprint Capacitor_SMD:C_0402_1005Metric -> Capacitor_SMD:C_0603_1608Metric
- C5: value 10p -> 10u; footprint Capacitor_SMD:C_0402_1005Metric -> Capacitor_SMD:C_0805_2012Metric
- C52: value 18p -> 47u; footprint Capacitor_SMD:C_0402_1005Metric -> Capacitor_SMD:C_1206_3216Metric
- C58: value 100n -> 47u; footprint Capacitor_SMD:C_0402_1005Metric -> Capacitor_SMD:C_1206_3216Metric
- C59: value DNP -> 100n; footprint Capacitor_SMD:C_0603_1608Metric -> Capacitor_SMD:C_0402_1005Metric
- C60, C61: value 100p -> 15p; moved to F.Cu
- C63: value DNP -> 100n; footprint Capacitor_SMD:C_0603_1608Metric -> Capacitor_SMD:C_0402_1005Metric; moved to F.Cu
- C64: value 10u -> 100n; footprint Capacitor_SMD:C_0805_2012Metric -> Capacitor_SMD:C_0402_1005Metric
- C66: value 2.2u -> 4.7u; moved to F.Cu
- C67, C68: value 100p -> 4.7u; footprint Capacitor_SMD:C_0402_1005Metric -> Capacitor_SMD:C_0603_1608Metric; moved to F.Cu
- C7: value 10p -> DNP; footprint Capacitor_SMD:C_0402_1005Metric -> Capacitor_SMD:C_0805_2012Metric
- C76, C93, C94: value 10u -> 2.2u; footprint Capacitor_SMD:C_0805_2012Metric -> Capacitor_SMD:C_0603_1608Metric; moved to F.Cu
- C77: value 10n -> 1u; footprint Capacitor_SMD:C_0402_1005Metric -> Capacitor_SMD:C_0603_1608Metric; moved to F.Cu
- C78: value 10n -> 100p; moved to F.Cu
- C79, C80: value 100u -> 100p; footprint Capacitor_Tantalum_SMD:CP_EIA-7343-31_Kemet-D -> Capacitor_SMD:C_0402_1005Metric; moved to F.Cu
- C81, C83: value 10u -> 100p; footprint Capacitor_SMD:C_0805_2012Metric -> Capacitor_SMD:C_0402_1005Metric; moved to F.Cu
- C82: value 100n -> 100p; footprint Capacitor_SMD:C_0805_2012Metric -> Capacitor_SMD:C_0402_1005Metric; moved to F.Cu
- C84, C87, C88, C90: value 10u -> 1u; footprint Capacitor_SMD:C_0805_2012Metric -> Capacitor_SMD:C_0603_1608Metric; moved to F.Cu
- C92: value 100n -> 2.2u; footprint Capacitor_SMD:C_0402_1005Metric -> Capacitor_SMD:C_0603_1608Metric; moved to F.Cu
- D2: value SS24FL -> Red; footprint Diode_SMD:D_SOD-123F -> LED_SMD:LED_0603_1608Metric
- D3: footprint Diode_SMD:D_SOD-123F -> fmcw:SOD-123F
- FB11: value 74279228600 -> BLM18PG181SH1D
- FB4: value CIC21P101NE -> BLM18PG181SH1D; footprint Inductor_SMD:L_0805_2012Metric -> Inductor_SMD:L_0603_1608Metric
- FB8: value BLM18PG181SH1D -> CIC21P101NE; footprint Inductor_SMD:L_0603_1608Metric -> Inductor_SMD:L_0805_2012Metric
- P1, P2: value SMA -> CONN_02X04; footprint fmcw:CONSMA003.062 -> Connector_PinHeader_2.54mm:PinHeader_2x04_P2.54mm_Vertical_SMD
- Q1: value RE1C002UN -> DNP(RE1C002UN)
- Q2: value DNP(RE1C002UN) -> RE1C002UN
- R1: value 5.49k -> 49.9
- R10: value 10k -> 4.7k
- R11, R9: value 18 -> 4.7k
- R12: value 18 -> 1k
- R13, R15: value 33 -> 0; moved to F.Cu
- R14: value 10k -> 33
- R16: value 33 -> DNP; moved to F.Cu
- R17, R52, R54: value 49.9 -> 10k
- R18: value 1.5k -> 2.2k
- R19: value 5.11k -> 12k
- R2: value DNP -> 1k
- R21: value 22 -> 0
- R22: value 100 -> 1k
- R23: value 100 -> 33
- R24: value 240 -> 33; moved to F.Cu
- R25: value 10k -> 33; moved to F.Cu
- R26: value 2.8k -> 4.7k; moved to F.Cu
- R27: value 33 -> 10k; moved to F.Cu
- R28: value 4.99k -> 49.9
- R29: value 20k -> 49.9; moved to F.Cu
- R3: value 470k -> 1k
- R30: value 274k -> 49.9
- R31: value 30.1k -> 49.9; moved to F.Cu
- R32: value 3.57k -> 0; moved to F.Cu
- R33: value 1.15k -> DNP; moved to F.Cu
- R39: value 47k -> 3.09k
- R4: value 3.09k -> 33
- R40: value DNP -> 4.7k
- R45: value 1.87k -> 1.5k
- R46: value 1.5k -> 10k
- R47: value 3.57k -> 100; footprint Resistor_SMD:R_0402_1005Metric -> Resistor_SMD:R_0603_1608Metric
- R48: value 1.15k -> 49.9
- R49: value 2k -> 100
- R5: value 4.7k -> 33
- R50: value DNP -> 100
- R51: value 49.9 -> 240
- R53: value 49.9 -> 2.8k
- R55: value 549 -> 5.11k
- R56: value 549 -> 4.99k
- R57: value 549 -> 20k
- R58: value 549 -> 68k
- R59: value 8.2k -> 274k
- R6: value 4.7k -> 240
- R60: value 8.2k -> 30.1k
- R61: value 8.2k -> 1.87k
- R62: value 8.2k -> 1.5k
- R63, R65: value DNP -> 3.57k
- R64, R66: value DNP -> 1.15k
- R67: value DNP -> 2k
- R69: value DNP -> 49.9
- R7: value 4.7k -> DNP
- R70: value 0 -> 49.9
- R71: value 12k -> 49.9
- R72: value 1k -> 49.9
- R73: value 10k -> 549
- R74, R75, R76: value DNP -> 549
- R77, R78: value DNP -> 8.2k
- R79: value 2.2k -> 8.2k
- R8: value 470k -> 0
- R80: value 0 -> 8.2k
- U1: value ADF4158 -> LP5907MFX-3.3; footprint Package_DFN_QFN:WQFN-24-1EP_4x4mm_P0.5mm_EP2.7x2.7mm -> Package_TO_SOT_SMD:SOT-23-5
- U10: value HMC431LP4 -> LP5907MFX-3.0; footprint Package_DFN_QFN:VQFN-24-1EP_4x4mm_P0.5mm_EP2.45x2.45mm -> Package_TO_SOT_SMD:SOT-23-5
- U11: value SKY65404 -> LTC2292; footprint fmcw:XFDFN-6 -> Package_DFN_QFN:QFN-64-1EP_9x9mm_P0.5mm_EP7.15x7.15mm
- U12: value PAT1220-6dB -> ADF4158; footprint fmcw:PAT1220 -> Package_CSP:LFCSP-24-1EP_4x4mm_P0.5mm_EP2.5x2.5mm
- U13: value TRF37A73 -> TLV172DCK; footprint fmcw:DFN-8-1EP_2x2mm_Pitch0.5mm -> Package_TO_SOT_SMD:SOT-353_SC-70-5
- U14: value FT2232H -> PAT1220-3dB; footprint Package_QFP:LQFP-64_10x10mm_P0.5mm -> RF_Converter:RF_Attenuator_Susumu_PAT1220
- U15: value SMA -> HMC431LP4; footprint fmcw:CONSMA003.062 -> Package_DFN_QFN:QFN-24-1EP_4x4mm_P0.5mm_EP2.8x2.8mm
- U16: value SKY65404 -> PD4859J5050S2HF; footprint fmcw:XFDFN-6 -> RF_Converter:Anaren_0805_2012Metric-6
- U17: value SE5004L -> PAT1220-5dB; footprint Package_DFN_QFN:QFN-20-1EP_4x4mm_P0.5mm_EP2.5x2.5mm -> RF_Converter:RF_Attenuator_Susumu_PAT1220
- U18: value TPS5420D -> SE5004L; footprint Package_SO:SOIC-8_3.9x4.9mm_P1.27mm -> Package_DFN_QFN:QFN-20-1EP_4x4mm_P0.5mm_EP2.5x2.5mm
- U19: value TPS5420D -> DC4759J5020AHF; footprint Package_SO:SOIC-8_3.9x4.9mm_P1.27mm -> RF_Converter:Anaren_0805_2012Metric-6
- U2: value LP5907-1.8 -> LP5907MFX-1.8
- U20: value LP5907-3.0 -> PAT1220-6dB; footprint Package_TO_SOT_SMD:SOT-23-5 -> RF_Converter:RF_Attenuator_Susumu_PAT1220
- U22: value TPS560200 -> TRF37A73; footprint Package_TO_SOT_SMD:SOT-23-5 -> Package_SON:WSON-8-1EP_2x2mm_P0.5mm_EP0.9x1.6mm
- U23: value TPS7A91 -> SKY65404; footprint fmcw:SON-10_2.5x2.5mm -> Package_DFN_QFN:Skyworks_DFN-6-1EP_1.5x1.5mm_P0.5mm_EP0.7x1.2mm
- U24: value TPS7A91 -> TRF37A73; footprint fmcw:SON-10_2.5x2.5mm -> Package_SON:WSON-8-1EP_2x2mm_P0.5mm_EP0.9x1.6mm
- U25: value TPS7A7001DDA -> SKY65404; footprint Package_SO:TI_SO-PowerPAD-8 -> Package_DFN_QFN:Skyworks_DFN-6-1EP_1.5x1.5mm_P0.5mm_EP0.7x1.2mm
- U26, U27: value 5400BL15B050E -> TPS5420D; footprint fmcw:5400BL15B050E -> Package_SO:SOIC-8_3.9x4.9mm_P1.27mm
- U28: value 5400BL15B050E -> TPS560200; footprint fmcw:5400BL15B050E -> Package_TO_SOT_SMD:SOT-23-5
- U29: value ADL5802 -> LP2985A-10DBVR; footprint Package_DFN_QFN:QFN-24-1EP_4x4mm_P0.5mm_EP2.6x2.6mm -> Package_TO_SOT_SMD:SOT-23-5
- U3: value PAT1220-6dB -> KT2520K-T; footprint fmcw:PAT1220 -> Oscillator:Oscillator_SMD_Kyocera_2520-6Pin_2.5x2.0mm
- U30: value XC7A15T-FTG256 -> TPS7A7001DDA; footprint fmcw:FTG256 -> Package_SO:TI_SO-PowerPAD-8
- U31: value 93LCxxB -> TPS7A91; footprint Package_SO:SOIC-8_3.9x4.9mm_P1.27mm -> Package_DFN_QFN:DFN-10-1EP_2.5x2.5mm_P0.5mm_EP1.2x2mm
- U32: footprint fmcw:SON-10_2.5x2.5mm -> Package_DFN_QFN:DFN-10-1EP_2.5x2.5mm_P0.5mm_EP1.2x2mm
- U34: value ADA4940-2 -> TPS7A91; footprint Package_DFN_QFN:WQFN-24-1EP_4x4mm_P0.5mm_EP2.7x2.7mm -> Package_DFN_QFN:DFN-10-1EP_2.5x2.5mm_P0.5mm_EP1.2x2mm
- U35: value ADA4940-2 -> 5400BL15B050E; footprint Package_DFN_QFN:WQFN-24-1EP_4x4mm_P0.5mm_EP2.7x2.7mm -> RF_Converter:Balun_Johanson_5400BL15B050E
- U39: value LP5907-3.0 -> ADA4940-2; footprint Package_TO_SOT_SMD:SOT-23-5 -> Package_CSP:LFCSP-24-1EP_4x4mm_P0.5mm_EP2.5x2.5mm
- U4: value KT2520K -> NC7SVU04P5X; footprint fmcw:KT2520K -> Package_TO_SOT_SMD:SOT-353_SC-70-5
- U5: value NC7S04P5X -> NB3N551; footprint Package_TO_SOT_SMD:SOT-353_SC-70-5 -> Package_DFN_QFN:DFN-8-1EP_2x2mm_P0.5mm_EP0.8x1.2mm
- U6: value NB3N551 -> XC7A15T-FTG256; footprint fmcw:DFN-8 -> fmcw:FTG256
- U7: value TLV172DCK -> W25Q32JV; footprint Package_TO_SOT_SMD:SOT-353_SC-70-5 -> Package_DFN_QFN:DFN-8-1EP_6x5mm_P1.27mm_EP3.4x4.3mm
- U8: value LTC2292 -> 93LCxxB; footprint Package_DFN_QFN:QFN-64-1EP_9x9mm_P0.5mm_EP4.85x4.85mm -> Package_SO:SOIC-8_3.9x4.9mm_P1.27mm
- U9: value TRF37A73 -> FT2232H; footprint fmcw:DFN-8-1EP_2x2mm_Pitch0.5mm -> Package_QFP:LQFP-64_10x10mm_P0.5mm
- Y1: footprint Crystal:Crystal_SMD_Abracon_ABM10-4Pin_2.5x2.0mm -> fmcw:ABM10
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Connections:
- C10 pad 2: Net-(C10-Pad2) -> GND
- C100 pad 1: Net-(C100-Pad1) -> /3V3D
- C101 pad 1: /1V8 -> /3V3D
- C103 pad 1: /5V -> /3V3A
- C104 pad 1: /1V8 -> /3V3A
- C106 pad 1: /5V -> /3V3A
- C107 pad 2: /5V -> Net-(C107-Pad2)
- C108 pad 1: GND -> Net-(C108-Pad1)
- C108 pad 2: /mixer/5VF -> GND
- C109 pad 1: Net-(C109-Pad1) -> Net-(C108-Pad1)
- C109 pad 2: Net-(C109-Pad2) -> GND
- C11 pad 1: Net-(C11-Pad1) -> GND
- C11 pad 2: Net-(C11-Pad2) -> Net-(C10-Pad1)
- C111 pad 1: Net-(C111-Pad1) -> Net-(C108-Pad1)
- C111 pad 2: Net-(C111-Pad2) -> GND
- C113 pad 1: Net-(C113-Pad1) -> /5V
- C113 pad 2: Net-(C113-Pad2) -> GND
- C114 pad 1: Net-(C114-Pad1) -> Net-(C110-Pad1)
- C114 pad 2: Net-(C114-Pad2) -> GND
- C115 pad 1: GND -> /10V
- C115 pad 2: /mixer/5VF -> GND
- C116 pad 1: GND -> /3V0
- C116 pad 2: /mixer/5VF -> GND
- C117 pad 1: GND -> Net-(C117-Pad1)
- C117 pad 2: /mixer/5VF -> GND
- C118 pad 1: GND -> Net-(C117-Pad1)
- C118 pad 2: /mixer/5VF -> GND
- C119 pad 1: GND -> Net-(C117-Pad1)
- C119 pad 2: /mixer/5VF -> GND
- C12 pad 1: /1V8_OSC -> /3V3_INV
- C120 pad 1: GND -> Net-(C120-Pad1)
- C120 pad 2: /mixer/5VF -> GND
- C121 pad 1: GND -> /3V3A
- C121 pad 2: /mixer/5VF -> GND
- C122 pad 1: GND -> /5V
- C122 pad 2: /mixer/5VF -> GND
- C123 pad 1: GND -> /5V
- C123 pad 2: /mixer/5VF -> GND
- C124 pad 1: /if/IF1+ -> Net-(C124-Pad1)
- C124 pad 2: /if/IF1- -> Net-(C124-Pad2)
- C125 pad 1: /if/IF2- -> Net-(C125-Pad1)
- C125 pad 2: /if/IF2+ -> GND
- C126 pad 2: Net-(C126-Pad2) -> GND
- C127 pad 2: Net-(C127-Pad2) -> Net-(C124-Pad2)
- C128 pad 1: Net-(C128-Pad1) -> Net-(C126-Pad1)
- C128 pad 2: Net-(C126-Pad1) -> GND
- C129 pad 1: Net-(C129-Pad1) -> Net-(C126-Pad1)
- C129 pad 2: Net-(C126-Pad2) -> GND
- C13 pad 1: Net-(C13-Pad1) -> Net-(C10-Pad1)
- C13 pad 2: Net-(C13-Pad2) -> GND
- C130 pad 1: Net-(C130-Pad1) -> Net-(C126-Pad1)
- C130 pad 2: Net-(C127-Pad1) -> GND
- C131 pad 1: Net-(C131-Pad1) -> Net-(C126-Pad1)
- C131 pad 2: Net-(C127-Pad2) -> GND
- C132 pad 1: /ADC_VCM2 -> GND
- C132 pad 2: GND -> Net-(C125-Pad1)
- C133 pad 1: /ADC_VCM1 -> GND
- C133 pad 2: GND -> Net-(C125-Pad1)
- C134 pad 1: Net-(C134-Pad1) -> GND
- C134 pad 2: Net-(C134-Pad2) -> Net-(C125-Pad1)
- C135 pad 1: Net-(C135-Pad1) -> GND
- C135 pad 2: Net-(C135-Pad2) -> Net-(C125-Pad1)
- C136 pad 1: Net-(C136-Pad1) -> GND
- C136 pad 2: Net-(C136-Pad2) -> Net-(C125-Pad1)
- C137 pad 2: Net-(C137-Pad2) -> GND
- C138 pad 1: /3V3A -> GND
- C138 pad 2: GND -> Net-(C138-Pad2)
- C139 pad 1: /3V3A -> GND
- C139 pad 2: GND -> Net-(C138-Pad2)
- C14 pad 1: Net-(C10-Pad1) -> GND
- C14 pad 2: GND -> /1V8
- C140 pad 1: Net-(C140-Pad1) -> GND
- C140 pad 2: Net-(C140-Pad2) -> Net-(C138-Pad2)
- C141 pad 1: Net-(C141-Pad1) -> GND
- C141 pad 2: Net-(C141-Pad2) -> Net-(C138-Pad2)
- C142 pad 1: Net-(C142-Pad1) -> GND
- C142 pad 2: Net-(C142-Pad2) -> Net-(C138-Pad2)
- C143 pad 1: Net-(C143-Pad1) -> Net-(C138-Pad2)
- C143 pad 2: Net-(C143-Pad2) -> GND
- C144 pad 1: Net-(C144-Pad1) -> /5V
- C144 pad 2: Net-(C140-Pad1) -> GND
- C145 pad 1: Net-(C145-Pad1) -> /3V0
- C145 pad 2: Net-(C141-Pad1) -> GND
- C146 pad 2: Net-(C142-Pad1) -> GND
- C147 pad 2: Net-(C143-Pad1) -> /RF1
- C148 pad 1: /ADC_VCM1 -> Net-(C146-Pad1)
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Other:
- board size 123.2 x 49.5 mm -> 147.8 x 68.6 mm
